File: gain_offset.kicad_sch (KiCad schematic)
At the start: 28 parts, among them U3 AD8337BCPZ-REEL-ND, U4 LMH6551MA, U5 AD8337BCPZ-REEL-ND, U7 LMH6551MA

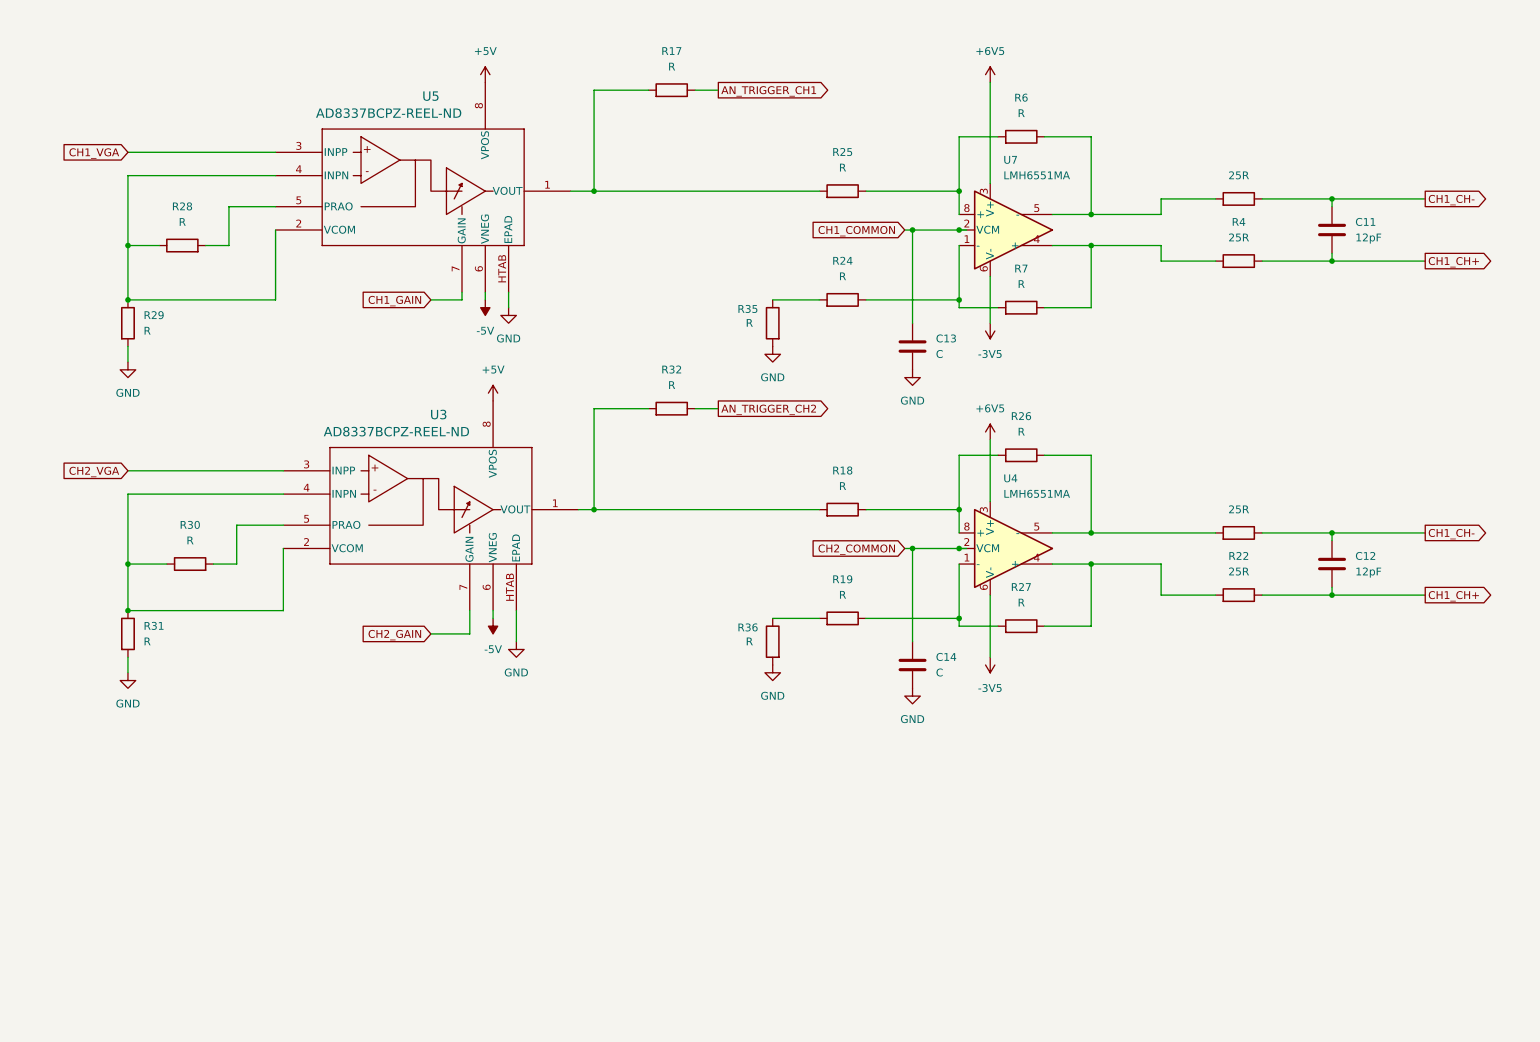
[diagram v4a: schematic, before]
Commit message: First version of analog path, without resistor values
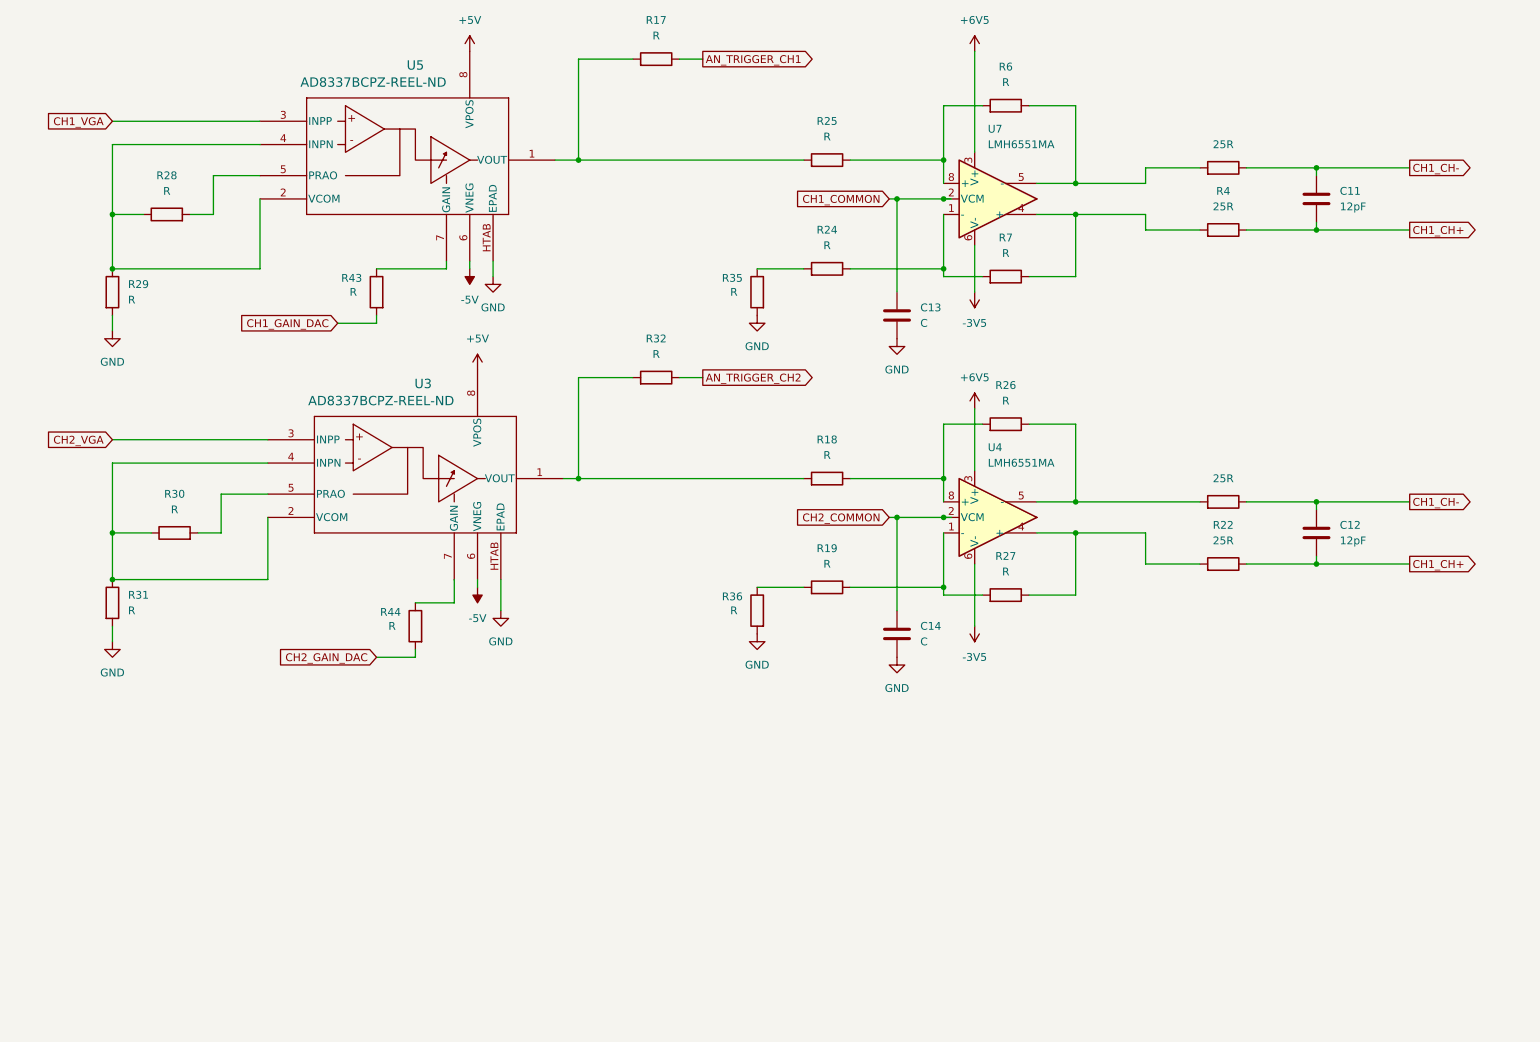
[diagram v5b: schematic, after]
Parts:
- added R43, R44: R, symbol Device:R
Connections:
- net CH1_GAIN: no longer names the net of U5.7 (GAIN)
- net CH1_GAIN: now also R43.1
- net CH2_GAIN: no longer names the net of U3.7 (GAIN)
- net CH2_GAIN: now also R44.1
- new net CH1_GAIN_DAC: R43.2
- new net CH2_GAIN_DAC: R44.2
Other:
- moved on the sheet: C11, C12, C13, C14, R17, R18, R19, R22, R24, R25, R26, R27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

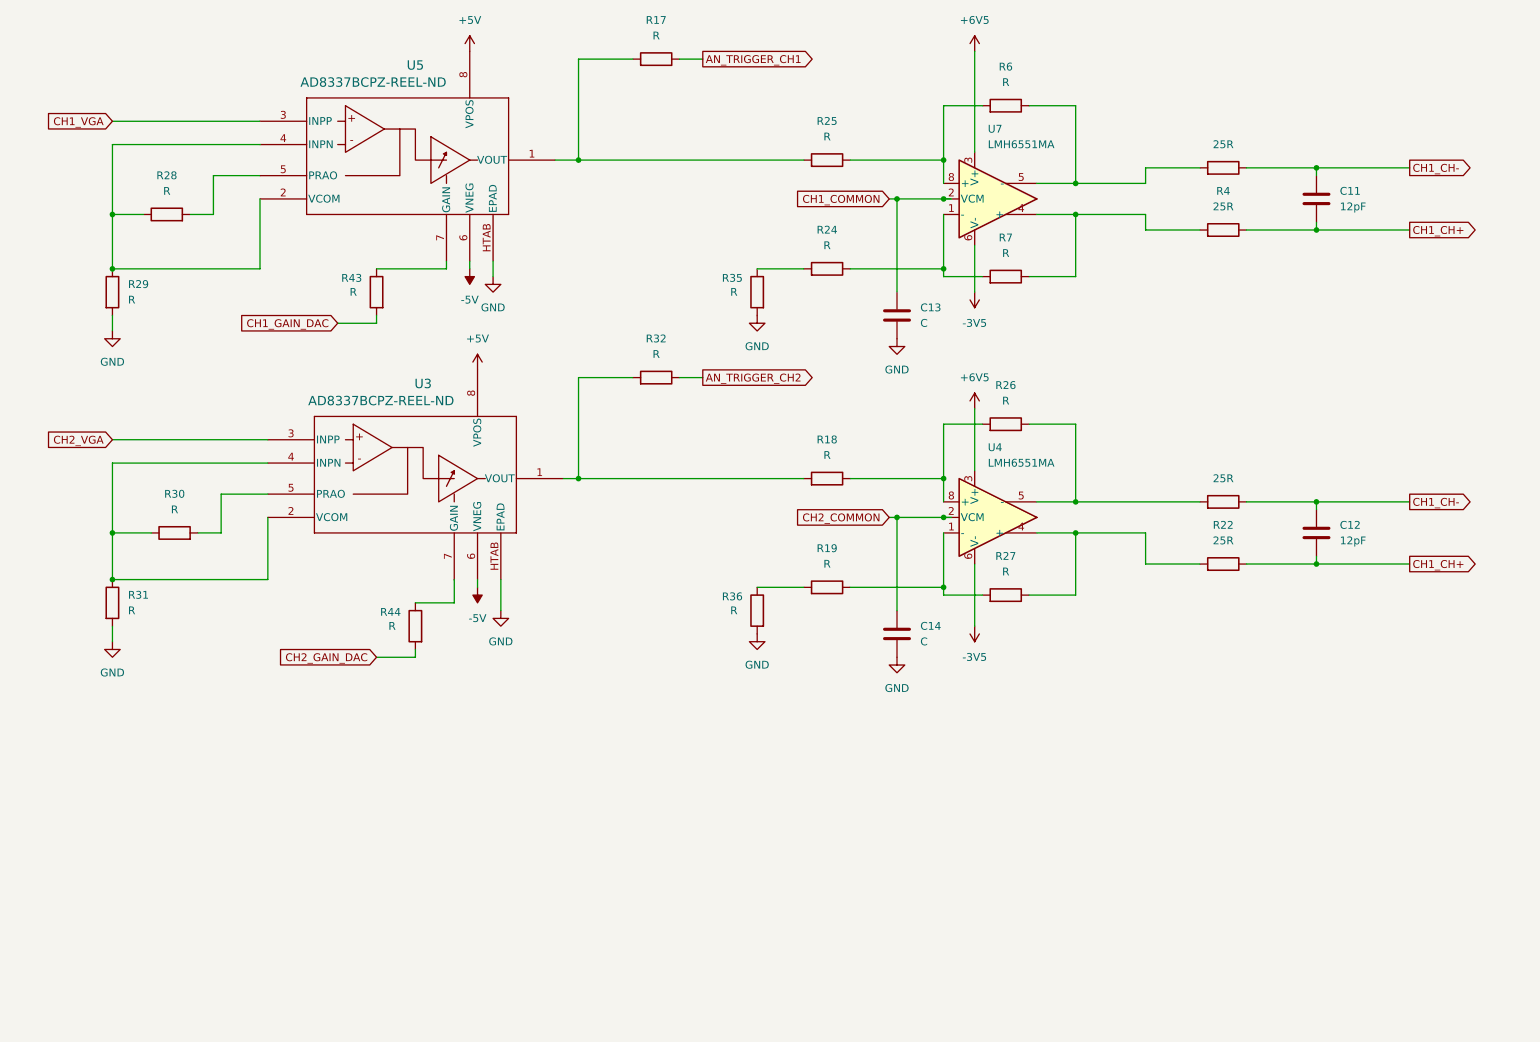
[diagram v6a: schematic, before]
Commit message: PCB edge, initial work on assigning footprints
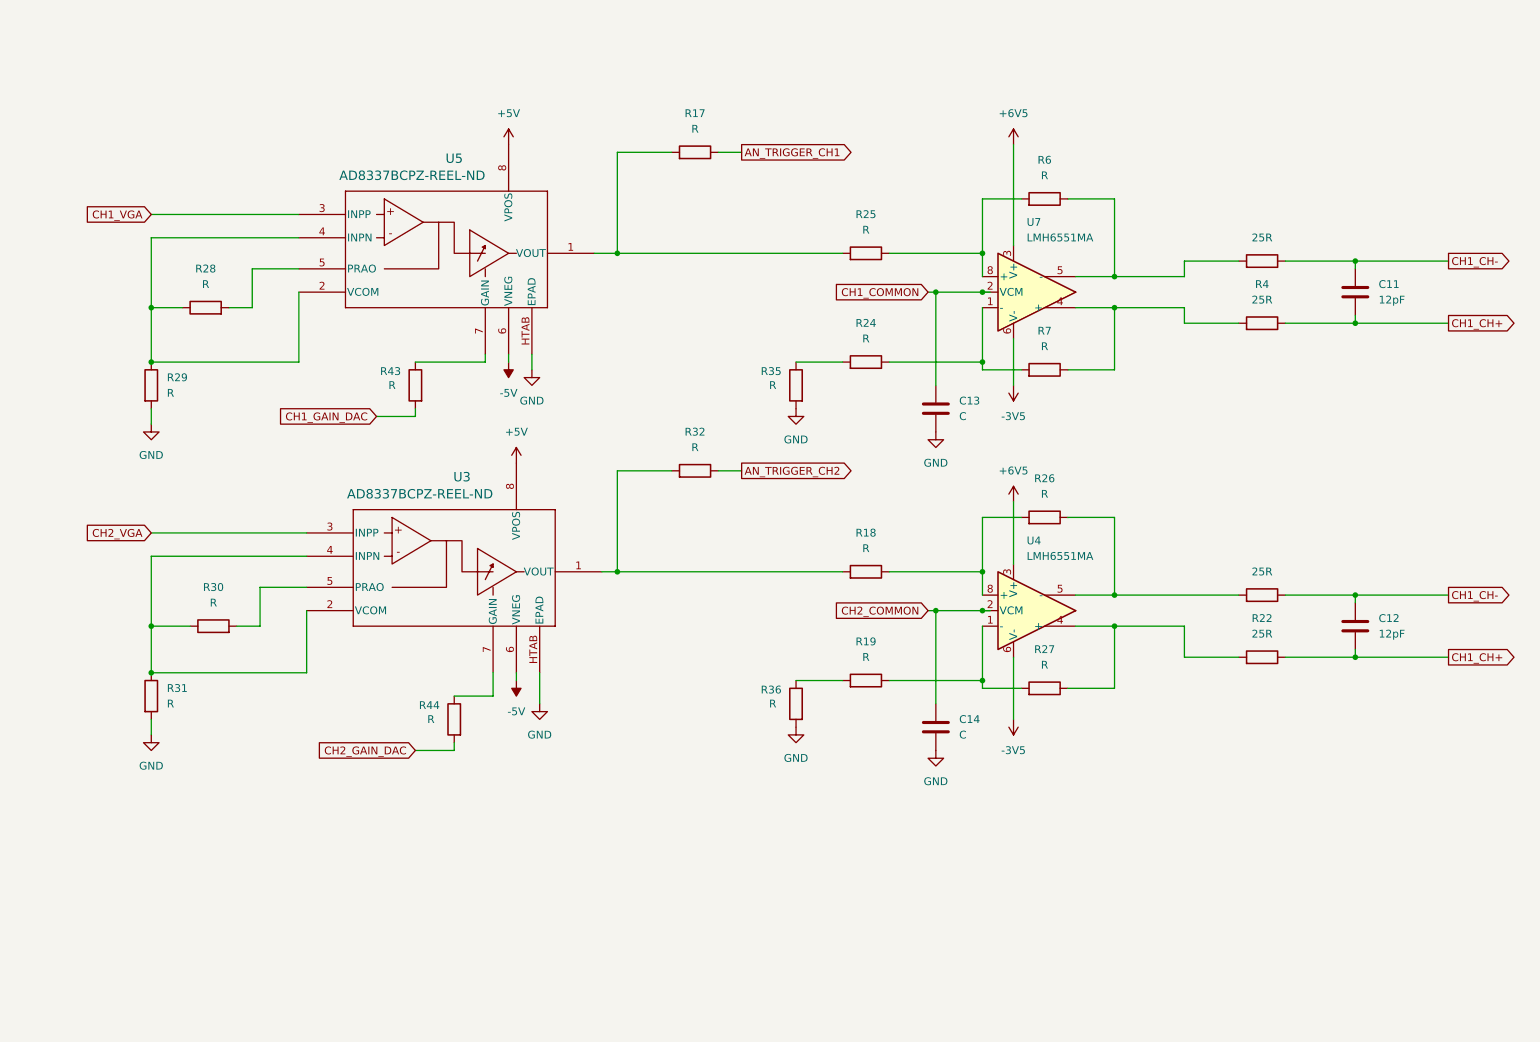
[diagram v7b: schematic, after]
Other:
- moved on the sheet: C11, C12, C13, C14, R17, R18, R19, R22, R24, R25, R26, R27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

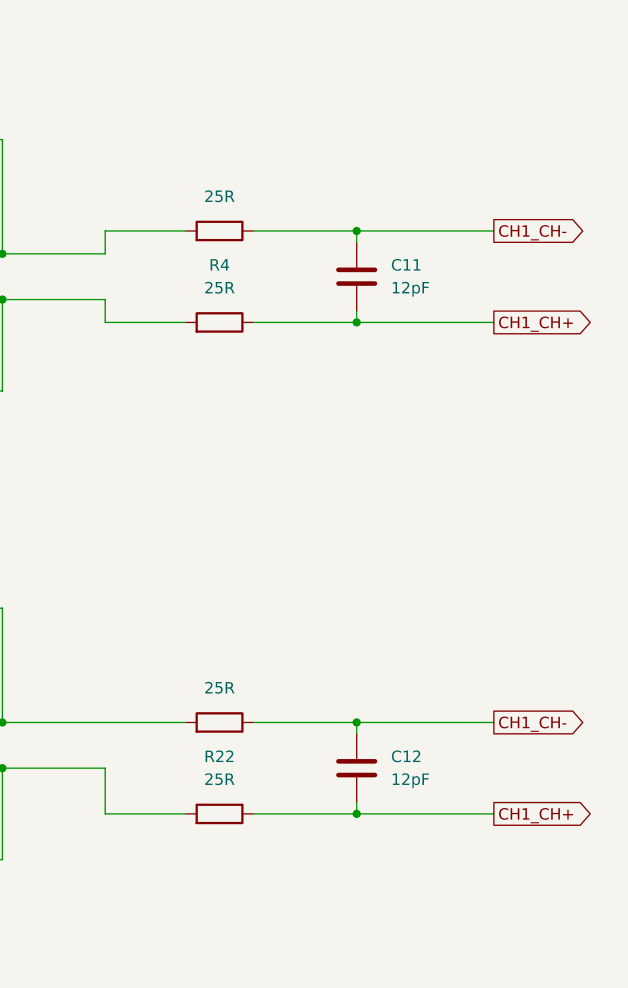
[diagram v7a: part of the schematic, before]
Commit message: Link up ADC to FPGA
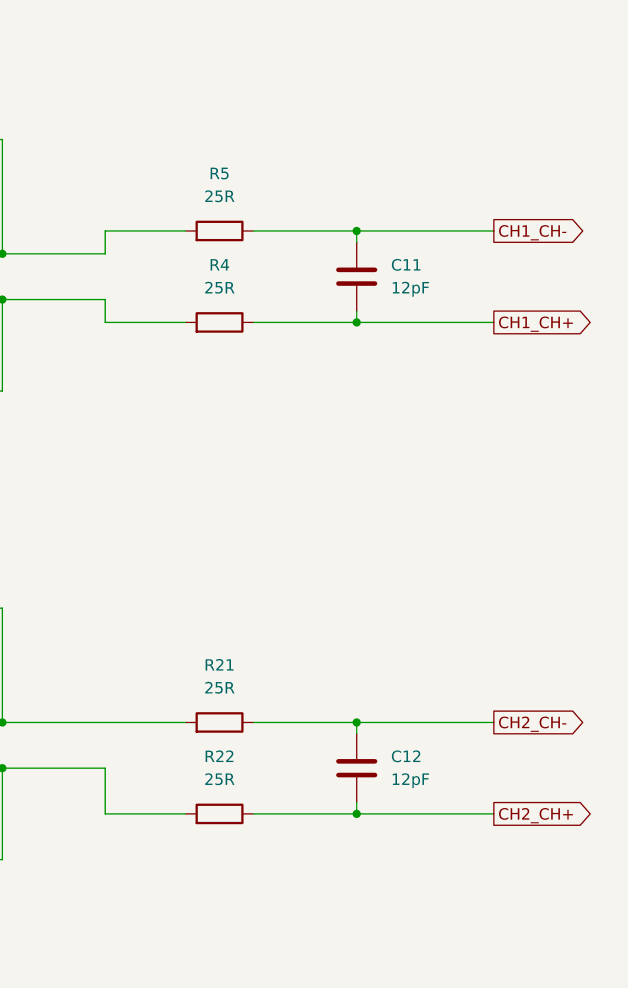
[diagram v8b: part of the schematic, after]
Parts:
- C11, C12: footprint (none) -> Capacitor_SMD:C_0603_1608Metric_Pad1.08x0.95mm_HandSolder
- R21, R22, R4, R5: footprint (none) -> Resistor_SMD:R_0402_1005Metric_Pad0.72x0.64mm_HandSolder
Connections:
- net CH1_CH+: no longer C12.2, R22.1
- net CH1_CH-: no longer C12.1, R21.1
- new net CH2_CH+: C12.2, R22.1
- new net CH2_CH-: C12.1, R21.1
